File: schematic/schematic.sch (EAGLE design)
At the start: 14 parts, among them J2 SJ-2523-SMT-TR

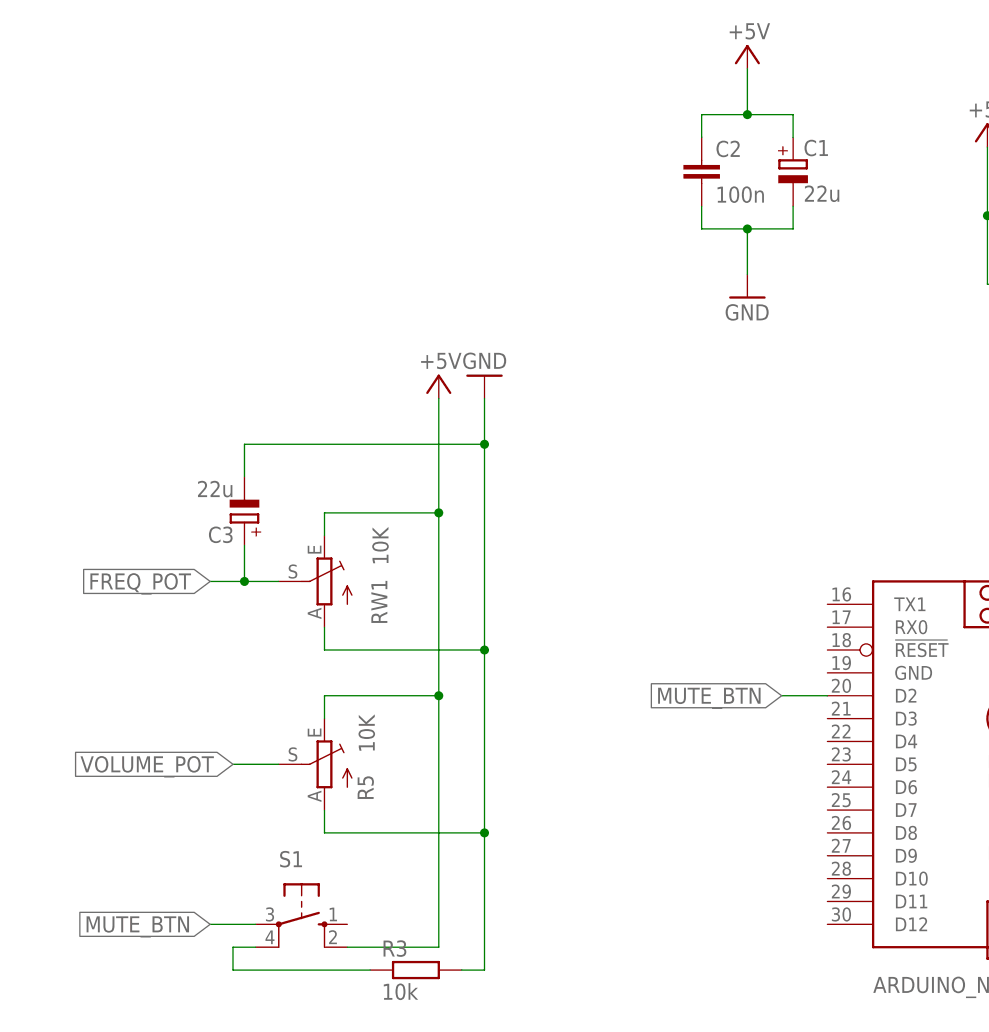
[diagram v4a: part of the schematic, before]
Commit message: Add simple ir receiver (#6)
* Add simple ir receiver

* Add IR receiver to schematic

* Add eagle backup files to gitignore

* Add controlling volume and freq remotely

* Rename variable

* Rename variable
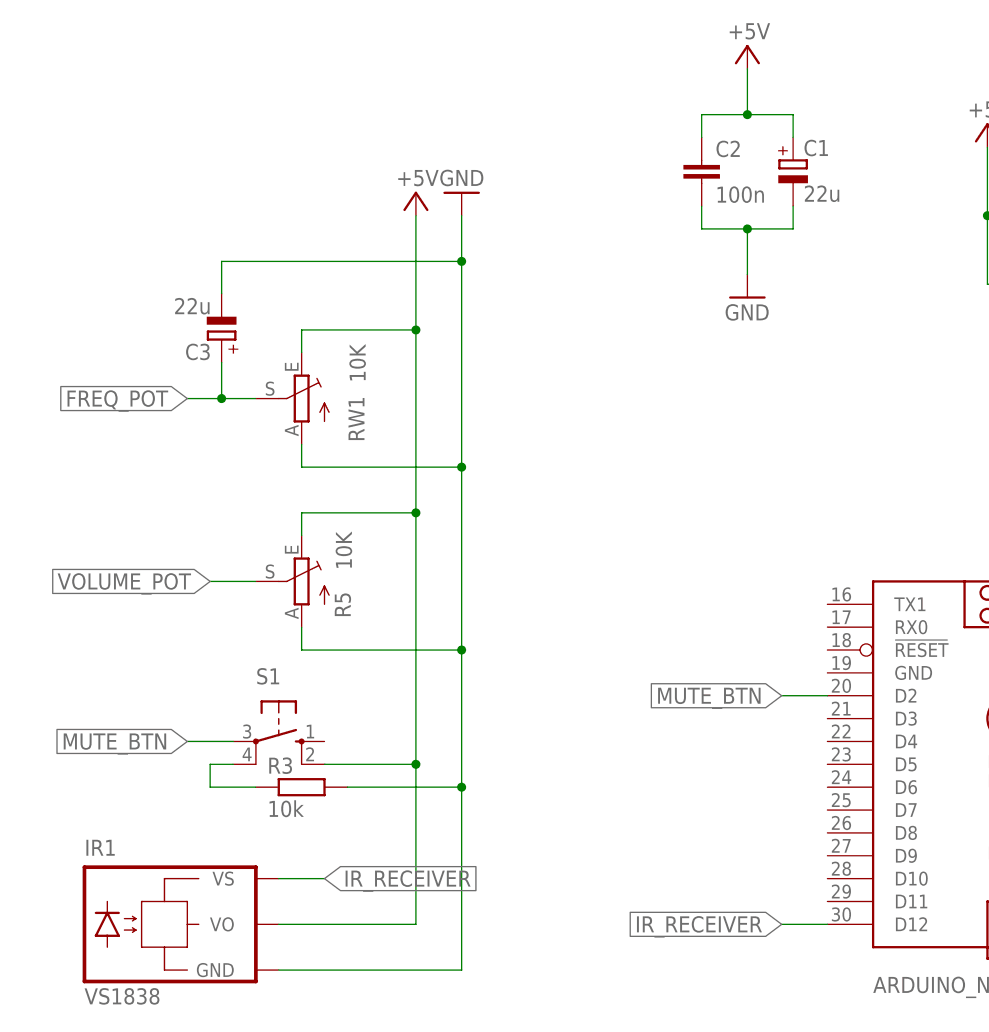
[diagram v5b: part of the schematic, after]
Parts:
- added IR1: VS1838, telefunken:TSOP1730TB1
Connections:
- new net IR_RECEIVER: ARDUINO_NANO_USER_CONTROLLER.D12, IR1.VS
- net +5V: now also IR1.VO
- net GND: now also IR1.GND
- net MUTE_BTN: no longer ARDUINO_NANO_USER_CONTROLLER.D12
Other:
- moved on the sheet: C3, R3, R5, RW1, S1

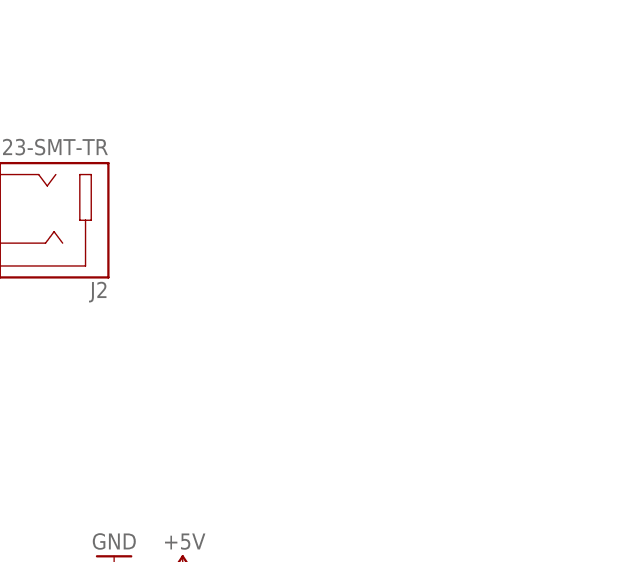
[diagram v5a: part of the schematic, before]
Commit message: Handle LCD (#7)
* Add Lcd class with simple interface

It uses LiquidCristal_I2C library
Simple init and write method

* Add Lcd to main.cpp, prints frequency

* Add schematic

* Move displaying freq to Controllers

* Apply CR suggestions

* Fix includes

* Set frequency as parameter of Lcd::displayFrequency()

* Update schematic

* Add displaying RDS
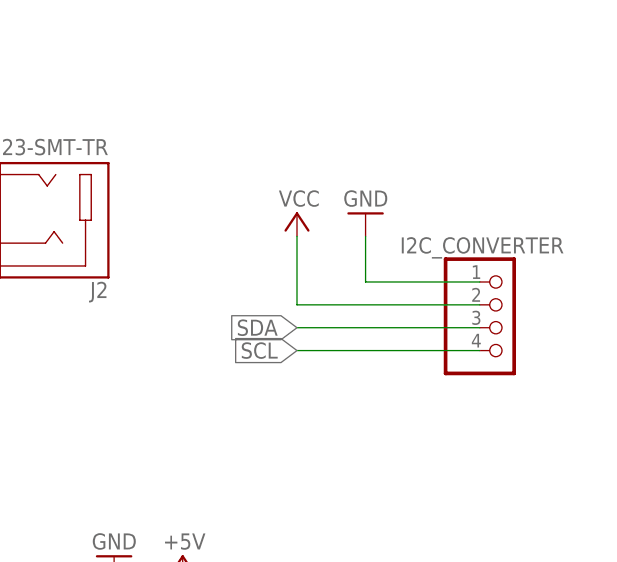
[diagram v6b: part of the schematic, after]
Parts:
- added I2C_CONVERTER: (no value), pinhead:PINHD-1X4
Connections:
- new net VCC: I2C_CONVERTER.2
- net GND: now also I2C_CONVERTER.1
- net SCL: now also I2C_CONVERTER.4
- net SDA: now also I2C_CONVERTER.3
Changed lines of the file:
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@@
 <schematic_group name="POWER_FILTRATION"/>
 <schematic_group name="CONTROLLERS"/>
+<schematic_group name="LCD"/>
 </groups>
 <parts>
@@
 <part name="R3" library="rcl" library_urn="urn:adsk.eagle:library:334" deviceset="R-EU_" device="0204/7" package3d_urn="urn:adsk.eagle:package:23498/2" value="10k"/>
 <part name="IR1" library="telefunken" library_urn="urn:adsk.eagle:library:383" deviceset="TSOP17*TB1" device="" package3d_urn="urn:adsk.eagle:package:27879/1" technology="30" value="VS1838"/>
+<part name="I2C_CONVERTER" library="pinhead" library_urn="urn:adsk.eagle:library:325" deviceset="PINHD-1X4" device="" package3d_urn="urn:adsk.eagle:package:22407/2"/>
+<part name="P+6" library="supply1" library_urn="urn:adsk.eagle:library:371" deviceset="VCC" device=""/>
+<part name="GND6" library="supply1" library_urn="urn:adsk.eagle:library:371" deviceset="GND" device=""/>
 </parts>
 <sheets>
@@
 <attribute name="VALUE" x="-100.33" y="21.59" size="1.778" layer="96"/>
 </instance>
+<instance part="I2C_CONVERTER" gate="A" x="162.56" y="104.14" smashed="yes" grouprefs="LCD">
+<attribute name="NAME" x="151.13" y="112.395" size="1.778" layer="95"/>
+<attribute name="VALUE" x="156.21" y="96.52" size="1.778" layer="96"/>
+</instance>
+<instance part="P+6" gate="VCC" x="139.7" y="116.84" smashed="yes" grouprefs="LCD">
+<attribute name="VALUE" x="142.24" y="119.38" size="1.778" layer="96" rot="R180"/>
+</instance>
+<instance part="GND6" gate="1" x="147.32" y="116.84" smashed="yes" rot="R180" grouprefs="LCD">
+<attribute name="VALUE" x="149.86" y="119.38" size="1.778" layer="96" rot="R180"/>
+</instance>
 </instances>
 <busses>
@@
 <label x="53.34" y="119.38" size="1.778" layer="95" rot="R180" xref="yes" grouprefs="RADIO_MODULE"/>
 </segment>
+<segment>
+<pinref part="I2C_CONVERTER" gate="A" pin="4"/>
+<wire x1="160.02" y1="101.6" x2="139.7" y2="101.6" width="0.1524" layer="91" grouprefs="LCD"/>
+<label x="139.7" y="101.6" size="1.778" layer="95" rot="R180" xref="yes" grouprefs="LCD"/>
+</segment>
 </net>
 <net name="SDA" class="0">
@@
 <wire x1="59.5" y1="122.46" x2="53.34" y2="122.46" width="0.1524" layer="91" grouprefs="RADIO_MODULE"/>
 <label x="53.34" y="122.428" size="1.778" layer="95" rot="R180" xref="yes" grouprefs="RADIO_MODULE"/>
+</segment>
+<segment>
+<pinref part="I2C_CONVERTER" gate="A" pin="3"/>
+<wire x1="160.02" y1="104.14" x2="139.7" y2="104.14" width="0.1524" layer="91" grouprefs="LCD"/>
+<label x="139.7" y="104.14" size="1.778" layer="95" rot="R180" xref="yes" grouprefs="LCD"/>
 </segment>
 </net>
@@
 <junction x="-58.42" y="45.72" grouprefs="CONTROLLERS"/>
 </segment>
+<segment>
+<pinref part="I2C_CONVERTER" gate="A" pin="1"/>
+<pinref part="GND6" gate="1" pin="GND"/>
+<wire x1="160.02" y1="109.22" x2="147.32" y2="109.22" width="0.1524" layer="91" grouprefs="LCD"/>
+<wire x1="147.32" y1="109.22" x2="147.32" y2="114.3" width="0.1524" layer="91" grouprefs="LCD"/>
+</segment>
 </net>
 <net name="+5V" class="0">
@@
 </segment>
 </net>
+<net name="VCC" class="0">
+<segment>
+<pinref part="I2C_CONVERTER" gate="A" pin="2"/>
+<pinref part="P+6" gate="VCC" pin="VCC"/>
+<wire x1="160.02" y1="106.68" x2="139.7" y2="106.68" width="0.1524" layer="91" grouprefs="LCD"/>
+<wire x1="139.7" y1="106.68" x2="139.7" y2="114.3" width="0.1524" layer="91" grouprefs="LCD"/>
+</segment>
+</net>

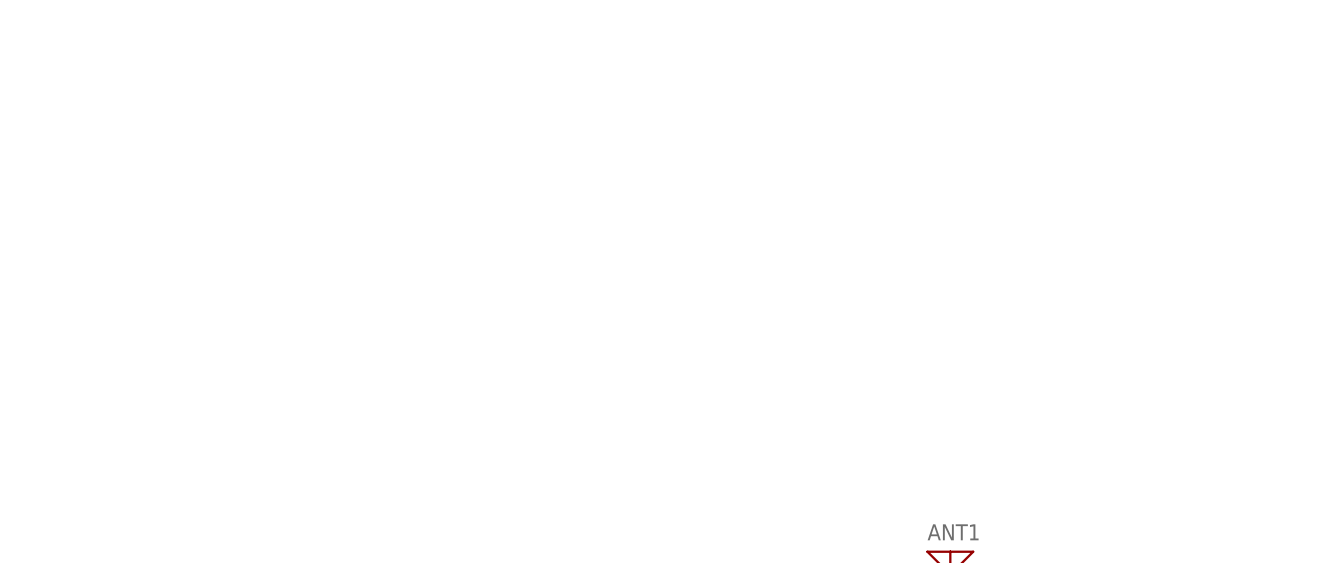
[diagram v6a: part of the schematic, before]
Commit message: Add Equalizer, there is sneaky bug
Add reading data from EQ
Add displaying bands on LCD
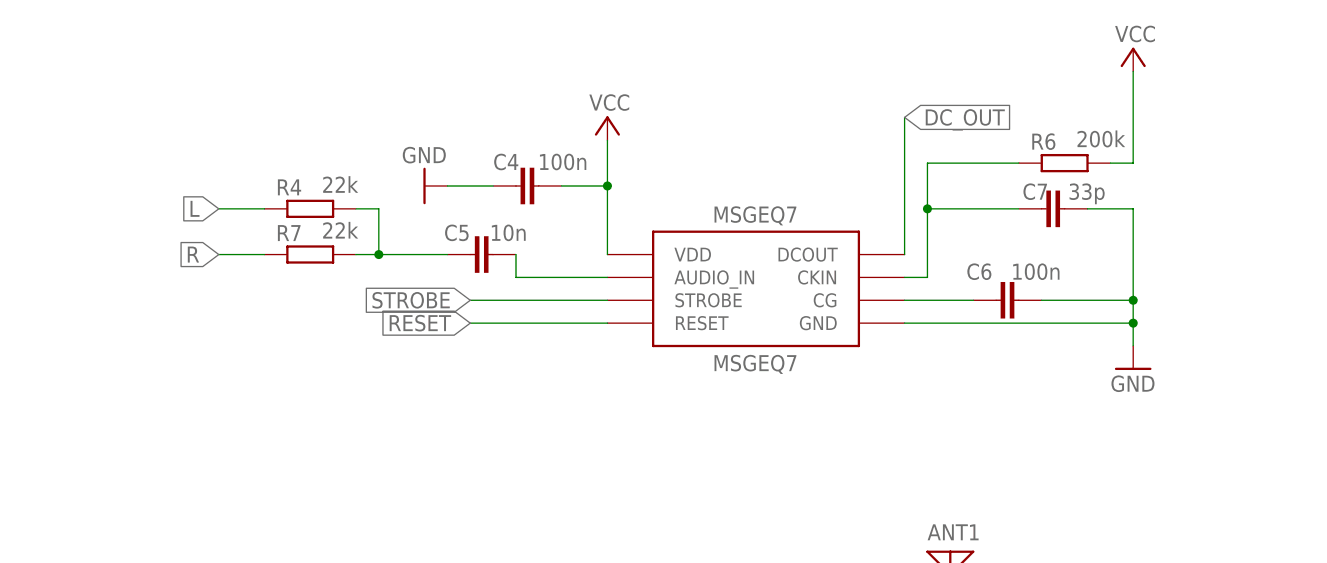
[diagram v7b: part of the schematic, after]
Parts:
- added C4, C6: 100n, rcl:C-EU025-025X050
- added C5: 10n, rcl:C-EU025-025X050
- added C7: 33p, rcl:C-EU025-025X050
- added MSGEQ7: MSGEQ7DIP, msgeq7:MSGEQ7DIP
- added R4, R7: 22k, rcl:R-EU_0204/7
- added R6: 200k, rcl:R-EU_0204/7
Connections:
- new net DC_OUT: MSGEQ7.DCOUT
- new net L: R4.1
- new net N$4: C5.1, R4.2, R7.2
- new net N$5: C7.2, MSGEQ7.CKIN, R6.1
- new net N$6: C5.2, MSGEQ7.AUDIO_IN
- new net N$7: C6.1, MSGEQ7.CG
- new net R: R7.1
- new net RESET: MSGEQ7.RESET
- new net STROBE: MSGEQ7.STROBE
- net GND: now also C4.2, C6.2, C7.1, MSGEQ7.GND
- net VCC: now also C4.1, MSGEQ7.VDD, R6.2

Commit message: Add labels to schematic
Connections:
- net DC_OUT: now also ARDUINO_NANO_USER_CONTROLLER.A3
- net RESET: now also ARDUINO_NANO_USER_CONTROLLER.D3
- net STROBE: now also ARDUINO_NANO_USER_CONTROLLER.D4
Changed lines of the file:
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@@
 <label x="40.64" y="162.56" size="1.778" layer="95" rot="R180" xref="yes" grouprefs="EQUALIZER"/>
+</segment>
+<segment>
+<pinref part="ARDUINO_NANO_USER_CONTROLLER" gate="G$1" pin="D4"/>
+<wire x1="-17.78" y1="50.8" x2="-22.86" y2="50.8" width="0.1524" layer="91" grouprefs="USER_CONTROLLER"/>
+<label x="-22.86" y="50.8" size="1.778" layer="95" rot="R180" xref="yes" grouprefs="USER_CONTROLLER"/>
 </segment>
 </net>
@@
 <label x="40.64" y="160.02" size="1.778" layer="95" rot="R180" xref="yes" grouprefs="EQUALIZER"/>
 </segment>
+<segment>
+<pinref part="ARDUINO_NANO_USER_CONTROLLER" gate="G$1" pin="D3"/>
+<wire x1="-17.78" y1="53.34" x2="-22.86" y2="53.34" width="0.1524" layer="91" grouprefs="USER_CONTROLLER"/>
+<label x="-22.86" y="53.34" size="1.778" layer="95" rot="R180" xref="yes" grouprefs="USER_CONTROLLER"/>
+</segment>
 </net>
 <net name="DC_OUT" class="0">
@@
 <label x="88.9" y="182.88" size="1.778" layer="95" xref="yes" grouprefs="EQUALIZER"/>
 </segment>
+<segment>
+<pinref part="ARDUINO_NANO_USER_CONTROLLER" gate="G$1" pin="A3"/>
+<wire x1="22.86" y1="45.72" x2="27.94" y2="45.72" width="0.1524" layer="91" grouprefs="USER_CONTROLLER"/>
+<label x="27.94" y="45.72" size="1.778" layer="95" xref="yes" grouprefs="USER_CONTROLLER"/>
+</segment>
 </net>
